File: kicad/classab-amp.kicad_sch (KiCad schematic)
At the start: 61 parts, among them Q1 BC547, Q10 MJL3218C, Q11 MJE350C, Q12 MJL1302C, Q13 BC547, Q14 BC557, Q2 BC547, Q3 BC557, Q4 BC557, Q5 BC547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

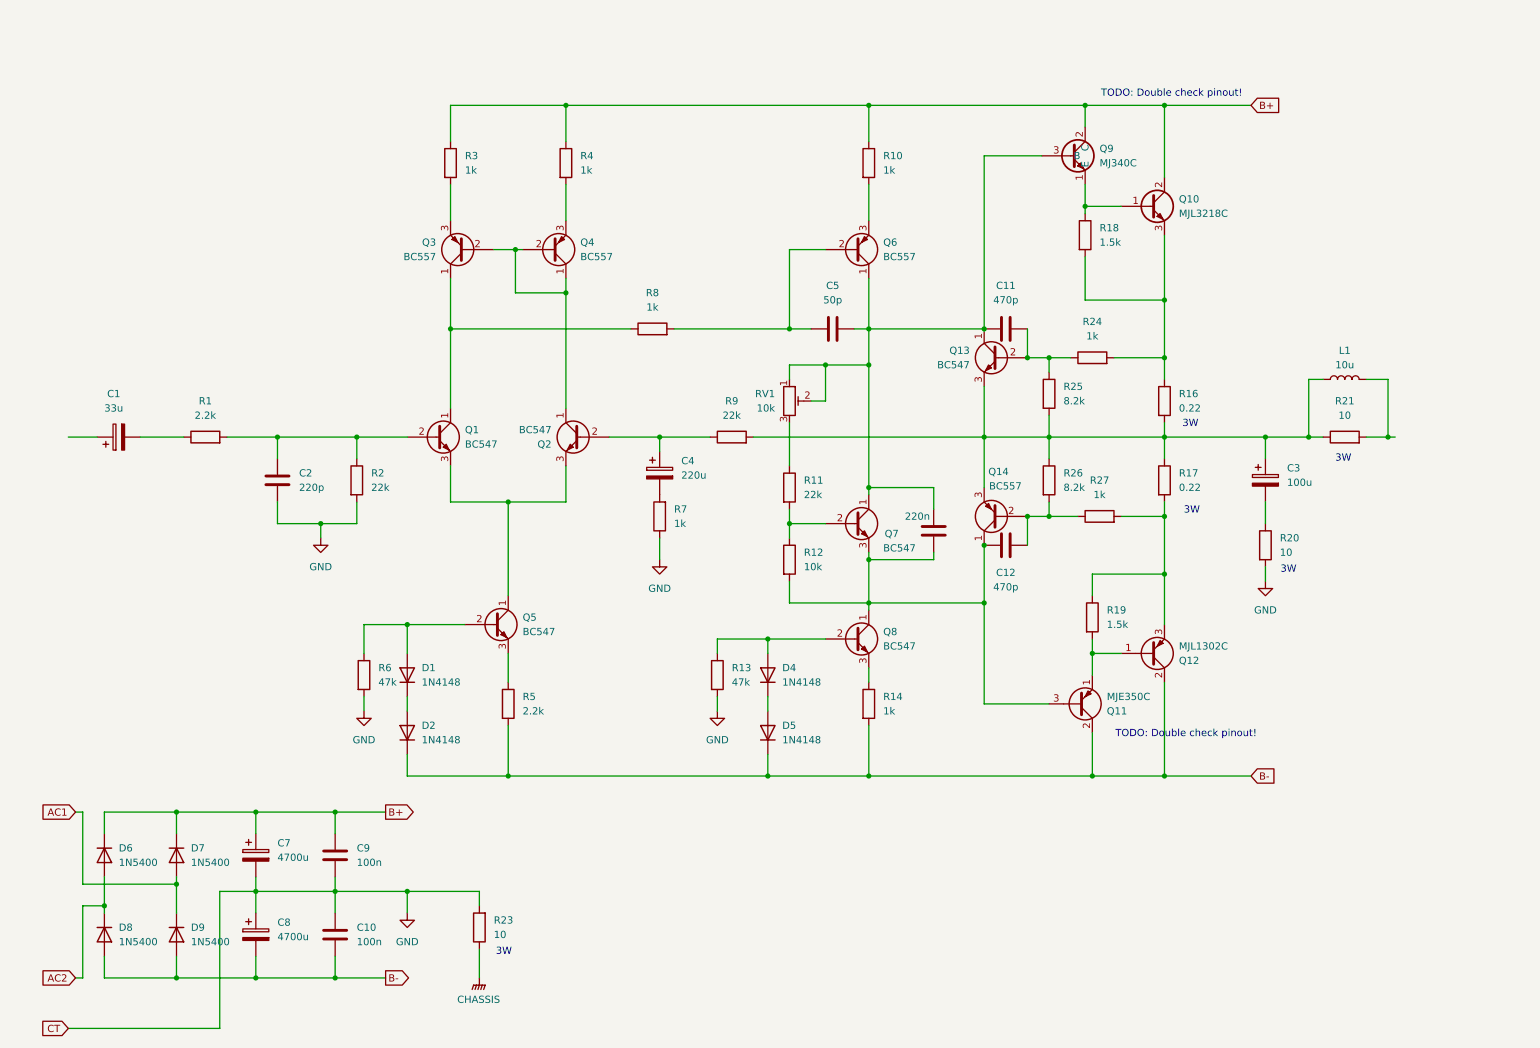
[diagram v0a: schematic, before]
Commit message: Fixed typos, tried to get SPICE working
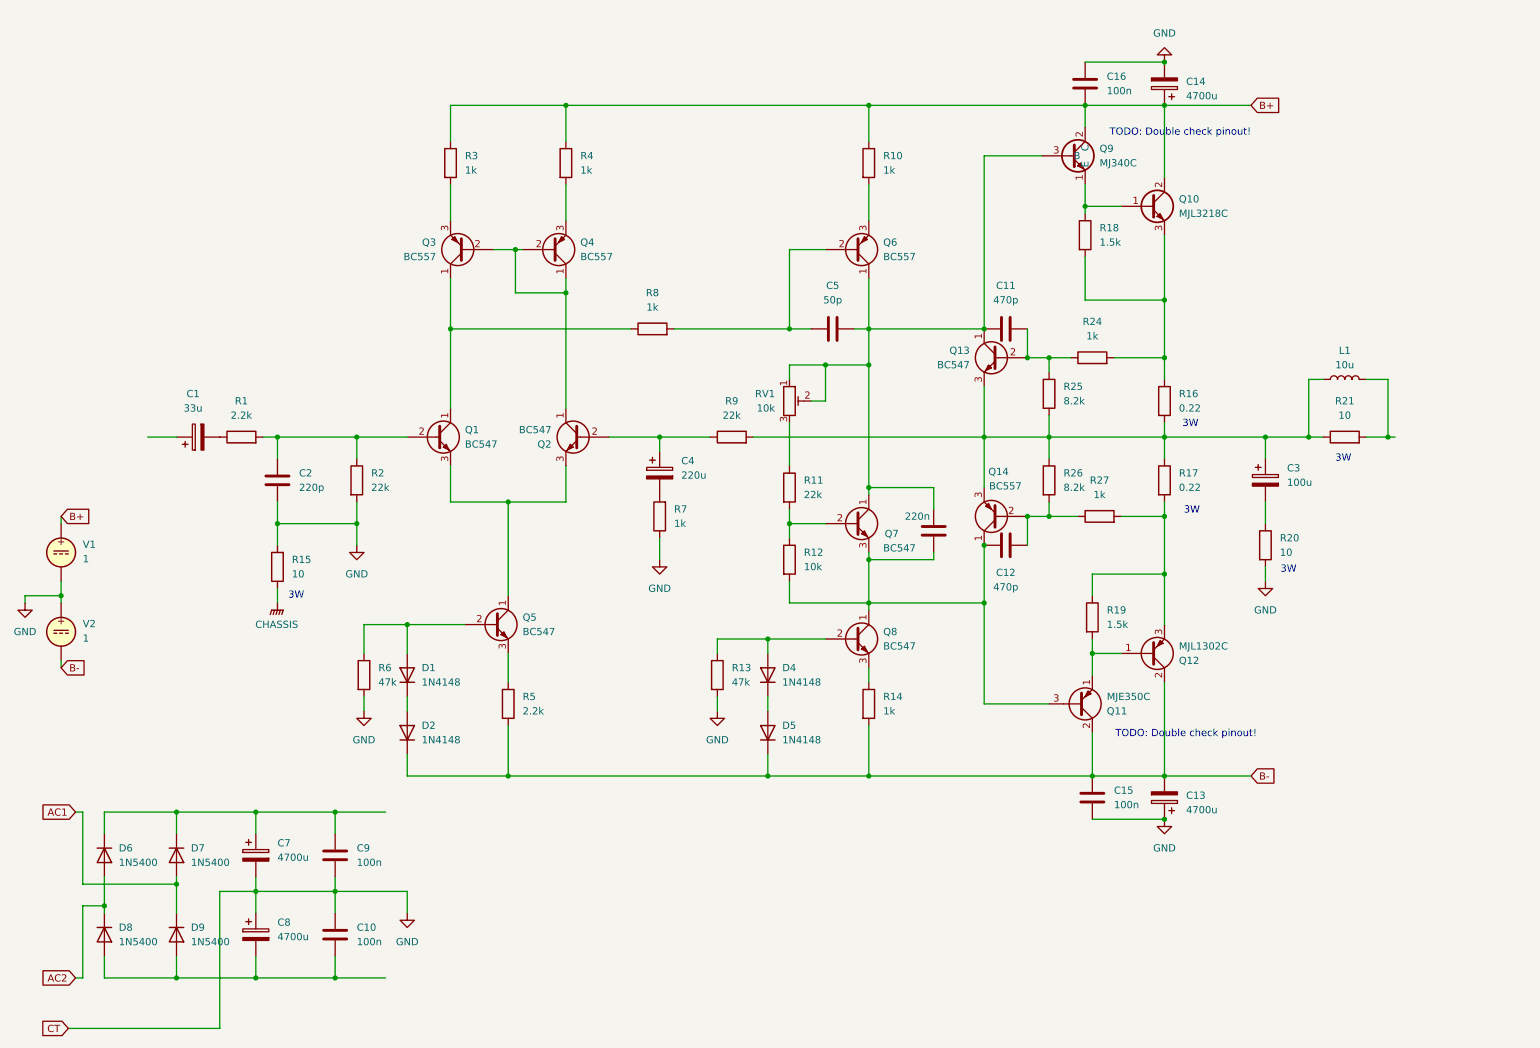
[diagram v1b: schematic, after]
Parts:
- removed R23: 10, symbol Device:R
- added C13, C14: 4700u, Capacitor_THT:CP_Radial_D18.0mm_P7.50mm, symbol Device:C_Polarized
- added C15, C16: 100n, symbol Device:C
- added R15: 10, symbol Device:R
- added V1, V2: 1, symbol Simulation_SPICE:VDC
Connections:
- net B+: now also C14.1, C16.2, V1.1; no longer C7.1, C9.1, D6.1 (K), D7.1 (K)
- net B-: now also C13.2, C15.1, V2.2; no longer C10.2, C8.2, D8.2 (A), D9.2 (A)
- net CHASSIS: now also R15.1
- net GND: now also C13.1, C14.2, C15.2, C16.1, R15.2, V1.2, V2.1
- new net: C10.2, C8.2, D8.2 (A), D9.2 (A)
- new net: C7.1, C9.1, D6.1 (K), D7.1 (K)
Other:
- moved on the sheet: C1, R1

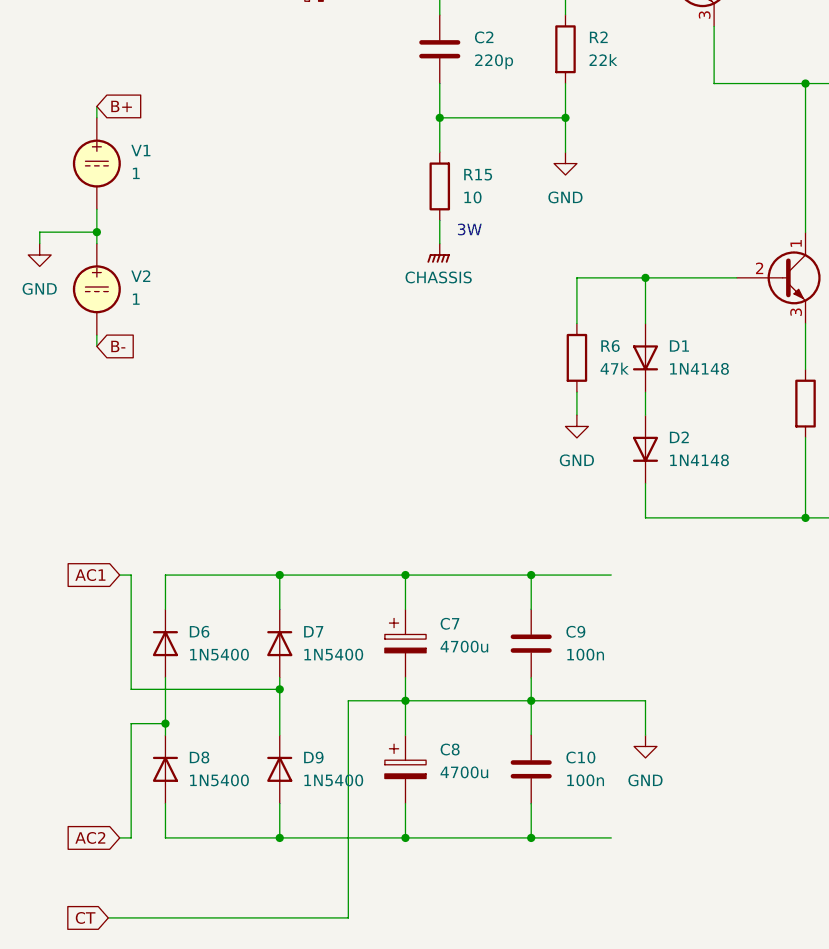
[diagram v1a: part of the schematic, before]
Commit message: Moved power supply to separate project
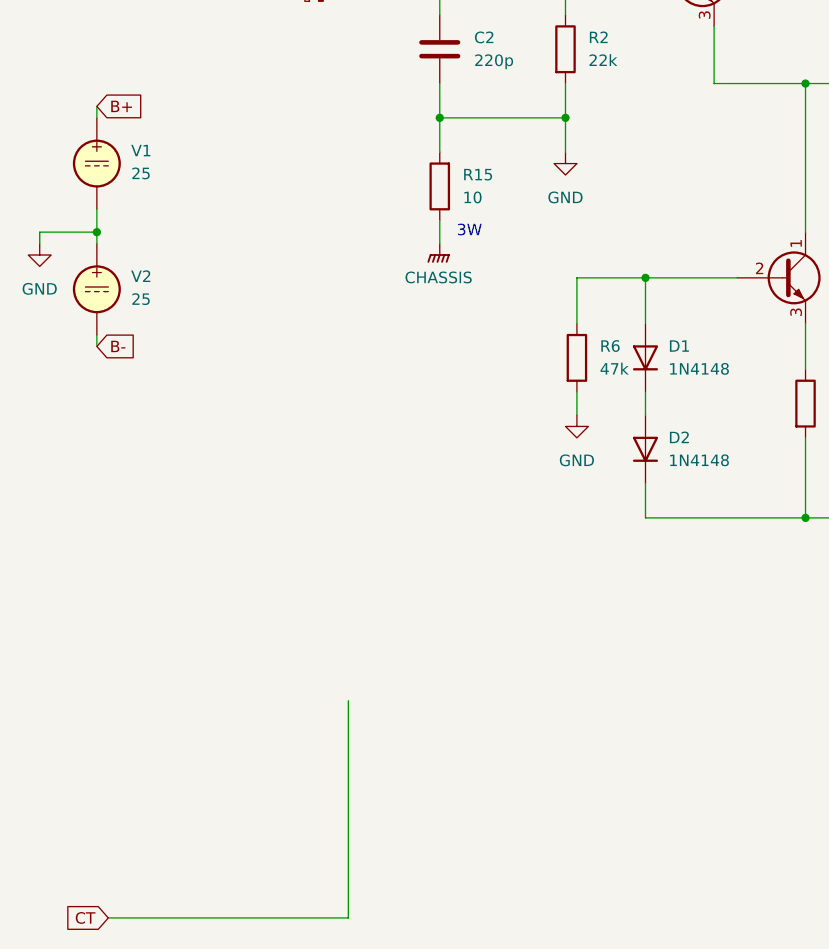
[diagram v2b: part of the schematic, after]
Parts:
- removed C10, C9: 100n, symbol Device:C
- removed C7, C8: 4700u, Capacitor_THT:CP_Radial_D18.0mm_P7.50mm, symbol Device:C_Polarized
- removed D6, D7, D8, D9: 1N5400, Diode_THT:D_DO-201AD_P15.24mm_Horizontal, symbol Diode:1N5400
- V1, V2: value 1 -> 25

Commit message: Improvements based on suggestions from various people
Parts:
- removed C3: 100u, Capacitor_THT:CP_Radial_D4.0mm_P1.50mm, symbol Device:C_Polarized
- removed Q11: MJE350C, Package_TO_SOT_THT:TO-126-3_Vertical, symbol Custom:MJE350C
- removed Q6: BC557, Package_TO_SOT_THT:TO-92_Inline, symbol Transistor_BJT:BC557
- removed Q8: BC547, Package_TO_SOT_THT:TO-92_Inline, symbol Transistor_BJT:BC547
- removed Q9: MJ340C, Package_TO_SOT_THT:TO-126-3_Vertical, symbol Custom:MJE340C
- added C3: 100n, symbol Device:C
- added D3, D6: 1N4001, Diode_THT:D_DO-41_SOD81_P10.16mm_Horizontal, symbol Diode:1N4001
- added Q11, Q6: BD140, Package_TO_SOT_THT:TO-126-3_Vertical, symbol Transistor_BJT:BD140
- added Q8, Q9: BD139, Package_TO_SOT_THT:TO-126-3_Vertical, symbol Transistor_BJT:BD139
- R12: value 10k -> 6.8k
- RV1: value 10k -> 5k; footprint Resistor_THT:R_Axial_DIN0204_L3.6mm_D1.6mm_P7.62mm_Horizontal -> (none)
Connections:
- net B+: now also Q9.2 (C)
- net B-: now also Q11.2 (C)
- net at R11.1: now also C5.2, C6.1, Q7.1 (C), D6.2 (A), Q6.2 (C), Q9.3 (B); no longer RV1.3
- net at L1.1, Q13.3 (E), Q14.3 (E)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: now also C3.1
- net at C6.2, Q7.3 (E), R12.2: now also D3.1 (K), Q11.3 (B), Q8.2 (C); no longer C12.1, Q14.1 (C)
- net at D4.2 (A), R13.1: now also Q8.3 (B)
- net at Q12.1 (B), R19.2: now also Q11.1 (E)
- net at Q7.2 (B), R11.2: now also RV1.1, RV1.2; no longer R12.1
- net SPEAKER: now reaches L1.2, R21.2
- net at R14.1: now also Q8.1 (E)
- net at Q10.1 (B), R18.1: now also Q9.1 (E)
- net at C5.1, R8.2: now also Q6.3 (B)
- net at R20.1: now also C3.2
- net INPUT: now reaches C1.1
- net at R10.2: now also Q6.1 (E)
- new net: C12.1, D3.2 (A), Q14.1 (C)
- new net: R12.1, RV1.3
- new net: C11.1, D6.1 (K), Q13.1 (C)
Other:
- note added: "BIAS TRIM"
- note removed: "TODO: Double check pinout!"
- moved on the sheet: L1, R12

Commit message: PCB layout
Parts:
- removed Q7: BC547, Package_TO_SOT_THT:TO-92_Inline, symbol Transistor_BJT:BC547
- added Q7: BD139, Package_TO_SOT_THT:TO-126-3_Vertical, symbol Transistor_BJT:BD139
- C11, C12, C15, C16, C5: footprint (none) -> Capacitor_THT:C_Rect_L7.2mm_W3.0mm_P5.00mm_FKS2_FKP2_MKS2_MKP2
- L1: footprint (none) -> Capacitor_THT:CP_Radial_D4.0mm_P1.50mm
- R15, R17, R20, R21: footprint (none) -> Resistor_THT:R_Axial_DIN0414_L11.9mm_D4.5mm_P15.24mm_Horizontal
- R16: footprint Resistor_THT:R_Axial_DIN0614_L14.3mm_D5.7mm_P25.40mm_Horizontal -> Resistor_THT:R_Axial_DIN0414_L11.9mm_D4.5mm_P15.24mm_Horizontal
- R24, R25, R26, R27: footprint (none) -> Resistor_THT:R_Axial_DIN0204_L3.6mm_D1.6mm_P7.62mm_Horizontal
- RV1: value 5k -> 10k; footprint (none) -> footprints:TRIM_T93YA103KT20
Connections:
- net at C5.2, C6.1, D6.2 (A)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: now also Q7.2 (C)
- net at C5.1, Q6.3 (B): now also R8.1; no longer R8.2
- net at R11.2, RV1.1, RV1.2: now also Q7.3 (B)
- net at C6.2, D3.1 (K), Q11.3 (B)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: now also Q7.1 (E)
- net at Q1.1 (C), Q3.1 (C): now also R8.2; no longer R8.1
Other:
- moved on the sheet: R8
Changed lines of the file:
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@@
 			)
 		)
-		(property "Footprint" "Resistor_THT:R_Axial_DIN0614_L14.3mm_D5.7mm_P25.40mm_Horizontal"
+		(property "Footprint" "Resistor_THT:R_Axial_DIN0414_L11.9mm_D4.5mm_P15.24mm_Horizontal"
 			(at 219.202 81.28 90)
 			(effects
@@
 			)
 		)
-		(property "Footprint" ""
+		(property "Footprint" "Capacitor_THT:C_Rect_L7.2mm_W3.0mm_P5.00mm_FKS2_FKP2_MKS2_MKP2"
 			(at 196.85 105.7148 0)
 			(effects
@@
 			)
 		)
-		(property "Footprint" ""
+		(property "Footprint" "Resistor_THT:R_Axial_DIN0204_L3.6mm_D1.6mm_P7.62mm_Horizontal"
 			(at 209.55 103.378 90)
 			(effects
@@
 			)
 		)
-		(property "Footprint" ""
+		(property "Footprint" "Resistor_THT:R_Axial_DIN0204_L3.6mm_D1.6mm_P7.62mm_Horizontal"
 			(at 198.882 95.25 90)
 			(effects
@@
 		(on_board yes)
 		(dnp no)
-		(fields_autoplaced yes)
 		(property "Reference" "RV1"
 			(at 152.4 106.6799 0)
@@
 			)
 		)
-		(property "Value" "5k"
+		(property "Value" "10k"
 			(at 152.4 109.2199 0)
 			(effects
@@
 			)
 		)
-		(property "Footprint" ""
+		(property "Footprint" "footprints:TRIM_T93YA103KT20"
 			(at 154.94 107.95 0)
 			(effects
@@
 	)
 	(symbol
-		(lib_id "Transistor_BJT:BC547")
-		(at 166.37 102.87 0)
-		(unit 1)
-		(exclude_from_sim no)
-		(in_bom yes)
-		(on_board yes)
-		(dnp no)
-		(property "Reference" "Q7"
-			(at 171.704 104.648 0)
-			(effects
-				(font
-					(size 1.27 1.27)
-				)
-				(justify left)
-			)
-		)
-		(property "Value" "BC547"
-			(at 171.45 107.188 0)
-			(effects
-				(font
-					(size 1.27 1.27)
-				)
-				(justify left)
-			)
-		)
-		(property "Footprint" "Package_TO_SOT_THT:TO-92_Inline"
-			(at 171.45 104.775 0)
-			(effects
-				(font
-					(size 1.27 1.27)
-					(italic yes)
-				)
-				(justify left)
-				(hide yes)
-			)
-		)
-		(property "Datasheet" "https://www.onsemi.com/pub/Collateral/BC550-D.pdf"
-			(at 166.37 102.87 0)
-			(effects
-				(font
-					(size 1.27 1.27)
-				)
-				(justify left)
-				(hide yes)
-			)
-		)
-		(property "Description" "0.1A Ic, 45V Vce, Small Signal NPN Transistor, TO-92"
-			(at 166.37 102.87 0)
-			(effects
-				(font
-					(size 1.27 1.27)
-				)
-				(hide yes)
-			)
-		)
-		(property "Sim.Library" "C:\\proj\\classab-amp\\spice\\BC547.mod"
-			(at 166.37 102.87 0)
-			(effects
-				(font
-					(size 1.27 1.27)
-				)
-				(hide yes)
-			)
-		)
-		(property "Sim.Name" "QBC547BP"
-			(at 166.37 102.87 0)
-			(effects
-				(font
-					(size 1.27 1.27)
-				)
-				(hide yes)
-			)
-		)
-		(property "Sim.Device" "NPN"
-			(at 166.37 102.87 0)
-			(effects
-				(font
-					(size 1.27 1.27)
-				)
-				(hide yes)
-			)
-		)
-		(property "Sim.Type" "GUMMELPOON"
-			(at 166.37 102.87 0)
-			(effects
-				(font
-					(size 1.27 1.27)
-				)
-				(hide yes)
-			)
-		)
-		(property "Sim.Pins" "1=C 2=B 3=E"
-			(at 166.37 102.87 0)
-			(effects
-				(font
-					(size 1.27 1.27)
-				)
-				(hide yes)
-			)
-		)
-		(pin "2"
-		)
-		(pin "3"
-		)
-		(pin "1"
-		)
-		(instances
-			(project "classab-amp"
-				(path "/856f1e14-388c-4d87-abe9-3c0c6310ec29"
-					(reference "Q7")
-					(unit 1)
-				)
-			)
-		)
-	)
-	(symbol
 		(lib_id "Device:R")
 		(at 220.98 95.25 0)
@@
 			)
 		)
-		(property "Footprint" ""
+		(property "Footprint" "Resistor_THT:R_Axial_DIN0414_L11.9mm_D4.5mm_P15.24mm_Horizontal"
 			(at 219.202 95.25 90)
 			(effects
@@
 			)
 		)
-		(property "Footprint" ""
+		(property "Footprint" "Resistor_THT:R_Axial_DIN0414_L11.9mm_D4.5mm_P15.24mm_Horizontal"
 			(at 252.73 89.408 90)
 			(effects
@@
 			)
 		)
-		(property "Footprint" ""
+		(property "Footprint" "Capacitor_THT:C_Rect_L7.2mm_W3.0mm_P5.00mm_FKS2_FKP2_MKS2_MKP2"
 			(at 209.2452 154.94 0)
 			(effects
@@
 	(symbol
 		(lib_id "Device:R")
-		(at 130.81 68.58 90)
+		(at 130.81 68.58 270)
 		(unit 1)
 		(exclude_from_sim no)
@@
 		)
 		(property "Footprint" "Resistor_THT:R_Axial_DIN0204_L3.6mm_D1.6mm_P7.62mm_Horizontal"
-			(at 130.81 70.358 90)
+			(at 130.81 66.802 90)
 			(effects
 				(font
@@
 			)
 		)
-		(property "Footprint" ""
+		(property "Footprint" "Resistor_THT:R_Axial_DIN0204_L3.6mm_D1.6mm_P7.62mm_Horizontal"
 			(at 198.882 80.01 90)
 			(effects
@@
 			)
 		)
-		(property "Footprint" ""
+		(property "Footprint" "Resistor_THT:R_Axial_DIN0204_L3.6mm_D1.6mm_P7.62mm_Horizontal"
 			(at 208.28 75.438 90)
 			(effects
@@
 			)
 		)
-		(property "Footprint" ""
+		(property "Footprint" "Capacitor_THT:CP_Radial_D4.0mm_P1.50mm"
 			(at 252.73 82.55 0)
 			(effects
@@
 			)
 		)
-		(property "Footprint" ""
+		(property "Footprint" "Capacitor_THT:C_Rect_L7.2mm_W3.0mm_P5.00mm_FKS2_FKP2_MKS2_MKP2"
 			(at 207.9752 29.21 0)
 			(effects
@@
 			)
 		)
-		(property "Footprint" ""
+		(property "Footprint" "Resistor_THT:R_Axial_DIN0414_L11.9mm_D4.5mm_P15.24mm_Horizontal"
 			(at 236.982 106.68 90)
 			(effects
@@
 			)
 		)
-		(property "Footprint" ""
+		(property "Footprint" "Capacitor_THT:C_Rect_L7.2mm_W3.0mm_P5.00mm_FKS2_FKP2_MKS2_MKP2"
 			(at 166.37 67.6148 0)
 			(effects
@@
 			)
 		)
-		(property "Footprint" ""
+		(property "Footprint" "Resistor_THT:R_Axial_DIN0414_L11.9mm_D4.5mm_P15.24mm_Horizontal"
 			(at 66.548 110.49 90)
 			(effects
@@
 			)
 		)
-		(property "Footprint" ""
+		(property "Footprint" "Capacitor_THT:C_Rect_L7.2mm_W3.0mm_P5.00mm_FKS2_FKP2_MKS2_MKP2"
 			(at 196.85 67.6148 0)
 			(effects
@@
 					(unit 1)
 				)
+			)
+		)
+	)
+	(symbol
+		(lib_id "Transistor_BJT:BD139")
+		(at 166.37 102.87 0)
+		(unit 1)
+		(exclude_from_sim no)
+		(in_bom yes)
+		(on_board yes)
+		(dnp no)
+		(fields_autoplaced yes)
+		(property "Reference" "Q7"
+			(at 171.45 101.5999 0)
+			(effects
+				(font
+					(size 1.27 1.27)
+				)
+				(justify left)
+			)
+		)
+		(property "Value" "BD139"
+			(at 171.45 104.1399 0)
+			(effects
+				(font
+					(size 1.27 1.27)
+				)
+				(justify left)
+			)
+		)
+		(property "Footprint" "Package_TO_SOT_THT:TO-126-3_Vertical"
+			(at 171.45 104.775 0)
+			(effects
+				(font
+					(size 1.27 1.27)
+					(italic yes)
+				)
+				(justify left)
+				(hide yes)
+			)
+		)
+		(property "Datasheet" "http://www.st.com/internet/com/TECHNICAL_RESOURCES/TECHNICAL_LITERATURE/DATASHEET/CD00001225.pdf"
+			(at 166.37 102.87 0)
+			(effects
+				(font
+					(size 1.27 1.27)
+				)
+				(justify left)
+				(hide yes)
+			)
+		)
+		(property "Description" "1.5A Ic, 80V Vce, Low Voltage Transistor, TO-126"
+			(at 166.37 102.87 0)
+			(effects
+				(font
+					(size 1.27 1.27)
+				)
+				(hide yes)
+			)
+		)
+		(pin "2"
+		)
+		(pin "3"
+		)
+		(pin "1"
+		)
+		(instances
+			(project ""
+				(path "/856f1e14-388c-4d87-abe9-3c0c6310ec29"
+					(reference "Q7")
+					(unit 1)
+				)

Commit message: v1.0
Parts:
- removed C6: 220n, symbol Device:C
- added J1: B-, TerminalBlock_Phoenix:TerminalBlock_Phoenix_MKDS-1,5-2-5.08_1x02_P5.08mm_Horizontal, symbol Connector:Screw_Terminal_01x01
- added J2: B+, symbol Connector:Screw_Terminal_01x01
- added J3: INPUT, TerminalBlock_4Ucon:TerminalBlock_4Ucon_1x02_P3.50mm_Horizontal, symbol Connector:Screw_Terminal_01x02
- C2, C3: footprint (none) -> Capacitor_THT:C_Rect_L7.2mm_W3.0mm_P5.00mm_FKS2_FKP2_MKS2_MKP2
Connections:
- net B+: now also J2.1 (Pin_1)
- net B-: now also J1.1 (Pin_1)
- net GND: now also J3.1 (Pin_1)
- net INPUT: now also J3.2 (Pin_2)

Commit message: Power supply
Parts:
- removed J1: B-, TerminalBlock_Phoenix:TerminalBlock_Phoenix_MKDS-1,5-2-5.08_1x02_P5.08mm_Horizontal, symbol Connector:Screw_Terminal_01x01
- removed J2: B+, symbol Connector:Screw_Terminal_01x01
- removed V1, V2: 25, symbol Simulation_SPICE:VDC
- added J1: SPEAKER, TerminalBlock_Phoenix:TerminalBlock_Phoenix_MKDS-1,5-2_1x02_P5.00mm_Horizontal, symbol Connector:Screw_Terminal_01x02
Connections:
- net GND: now also J1.2 (Pin_2)
- net SPEAKER: now also J1.1 (Pin_1)
- net LTP COM: now reaches Q2.1 (C), Q3.2 (B), Q4.1 (C), Q4.2 (B)
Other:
- moved on the sheet: J3, L1, R20, R21
